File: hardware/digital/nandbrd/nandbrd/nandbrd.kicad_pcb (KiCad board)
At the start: 2 copper layers, 46.9 x 59.8 mm, 14 parts, among them J1 Conn_01x20_Female, J2 Conn_01x20_Male, J3 Conn_01x04_Male, U1 BL652

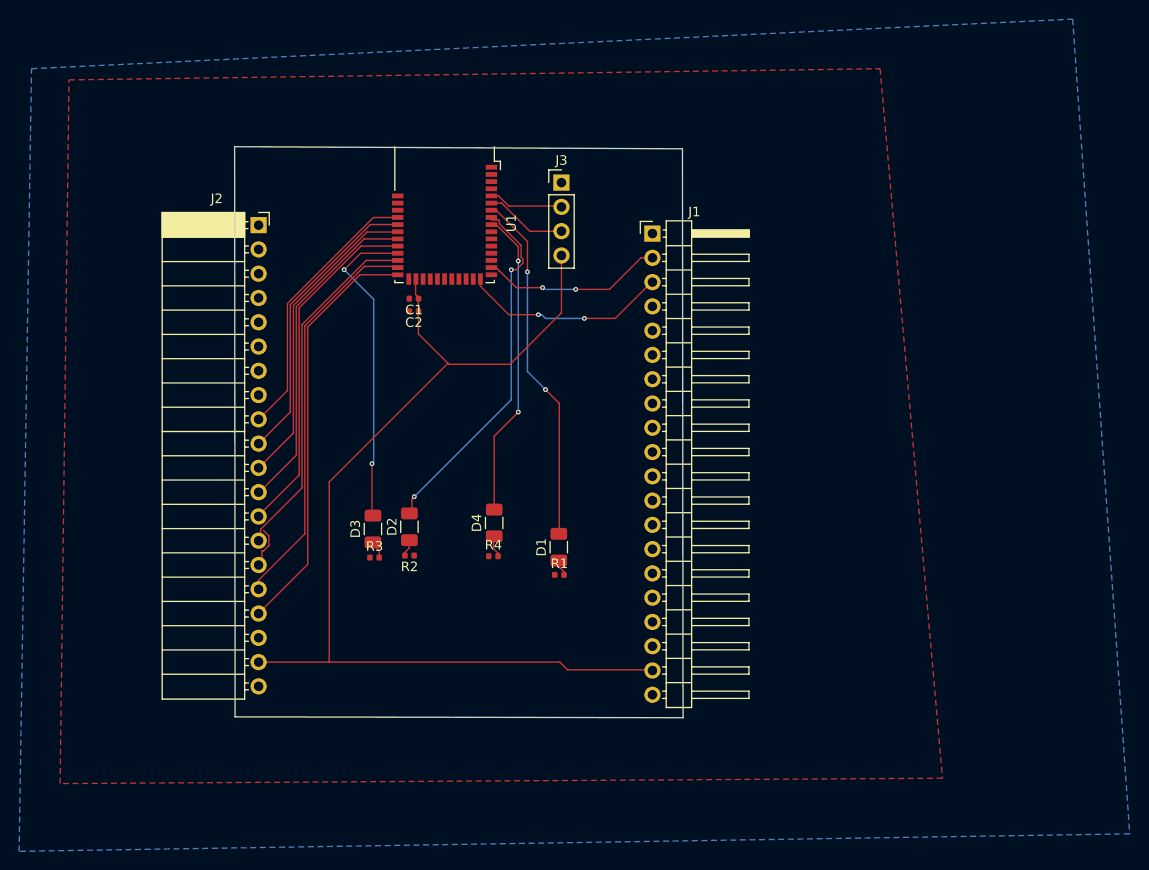
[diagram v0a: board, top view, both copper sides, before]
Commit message: started NAND brd layout. trying to use autorouter
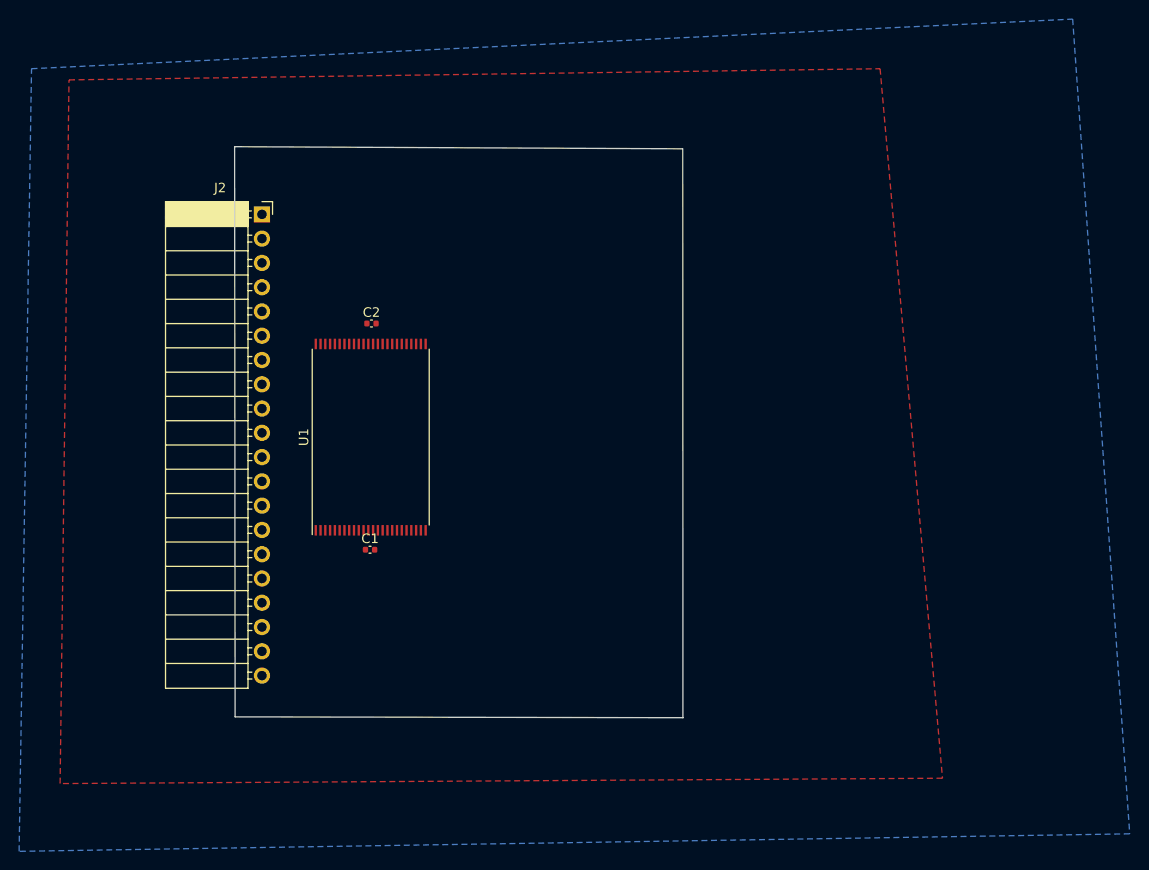
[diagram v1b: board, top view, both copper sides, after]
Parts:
- removed D1, D2, D3, D4: LED, Capacitor_SMD:C_1206_3216Metric
- removed J1: Conn_01x20_Female, Connector_PinHeader_2.54mm:PinHeader_1x20_P2.54mm_Horizontal
- removed J3: Conn_01x04_Male, Connector_PinHeader_2.54mm:PinHeader_1x04_P2.54mm_Vertical
- removed R1, R2, R3, R4: 10kOhm, Resistor_SMD:R_0402_1005Metric
- U1: value BL652 -> MT29F1G08ABAEAWP; footprint RF_Module:Laird_BL652 -> Package_SO:TSOP-I-48_18.4x12mm_P0.5mm
- moved C1 26.7 mm to (133.2, 78.0), turned to 0 degrees
- moved U1 23.7 mm to (133.3, 66.2), turned to 90 degrees
- moved C2 4.62 mm to (133.4, 54.3), turned to 0 degrees
- moved J2 1.18 mm to (121.9, 42.9)
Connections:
- C1 pad 1: +3V3 -> WP
- C2 pad 1: +3V3 -> WP
- J2 pad 10: Net-(J2-Pad10) -> GND
- J2 pad 11: Net-(J2-Pad11) -> D1
- J2 pad 12: Net-(J2-Pad12) -> D0
- J2 pad 13: Net-(J2-Pad13) -> GND
- J2 pad 14: Net-(J2-Pad14) -> CE
- J2 pad 16: Net-(J2-Pad16) -> CLE
- J2 pad 17: Net-(J2-Pad17) -> WE
- J2 pad 18: GND -> RE
- J2 pad 19: +3V3 -> ALE
- J2 pad 2: Net-(J2-Pad2) -> D7
- J2 pad 20: GND -> WP
- J2 pad 3: Net-(J2-Pad3) -> D6
- J2 pad 5: Net-(J2-Pad5) -> D5
- J2 pad 6: Net-(J2-Pad6) -> D4
- J2 pad 7: Net-(J2-Pad7) -> GND
- J2 pad 8: GND -> D3
- J2 pad 9: Net-(J2-Pad9) -> D2
- U1 pad 1: GND -> Net-(U1-Pad1)
- U1 pad 12: Net-(U1-Pad12) -> WP
- U1 pad 13: Net-(U1-Pad13) -> GND
- U1 pad 16: GND -> CLE
- U1 pad 17: Net-(J1-Pad3) -> ALE
- U1 pad 18: Net-(U1-Pad18) -> WE
- U1 pad 19: Net-(U1-Pad19) -> WP
- U1 pad 26: +3V3 -> Net-(U1-Pad26)
- U1 pad 27: GND -> Net-(U1-Pad27)
- U1 pad 28: Net-(J2-Pad17) -> Net-(U1-Pad28)
- U1 pad 29: Net-(J2-Pad16) -> D0
- U1 pad 30: Net-(J2-Pad14) -> D1
- U1 pad 31: Net-(D3-Pad2) -> D2
- U1 pad 32: Net-(J2-Pad13) -> D3
- U1 pad 33: Net-(J2-Pad12) -> Net-(U1-Pad33)
- U1 pad 34: Net-(J2-Pad11) -> Net-(U1-Pad34)
- U1 pad 35: Net-(J2-Pad10) -> Net-(U1-Pad35)
- U1 pad 36: Net-(J2-Pad9) -> GND
- U1 pad 37: Net-(U1-Pad37) -> WP
- U1 pad 39: GND -> Net-(U1-Pad39)
- U1 pad 7: Net-(D1-Pad2) -> (no net)
- U1 pad 8: Net-(D2-Pad2) -> RE
- U1 pad 9: Net-(D4-Pad2) -> CE
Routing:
- net +3V3: track 108.5 -> 0.00 mm
- net Net-(J2-Pad17): track 43.9 -> 0.00 mm
- net Net-(J2-Pad16): track 41.9 -> 0.00 mm
- net Net-(D2-Pad2): track 38.1 -> 0.00 mm, vias 2 -> 0
- net Net-(J2-Pad14): track 37.3 -> 0.00 mm
- net Net-(D1-Pad2): track 37.2 -> 0.00 mm, vias 2 -> 0
- net Net-(J2-Pad13): track 36.6 -> 0.00 mm
- net Net-(J2-Pad12): track 34.4 -> 0.00 mm
- net Net-(D3-Pad2): track 33.8 -> 0.00 mm, vias 2 -> 0
- net Net-(J2-Pad11): track 32.3 -> 0.00 mm
- net Net-(D4-Pad2): track 32.3 -> 0.00 mm, vias 2 -> 0
- net Net-(J2-Pad10): track 30.4 -> 0.00 mm
- net Net-(J2-Pad9): track 28.7 -> 0.00 mm
- net Net-(J1-Pad3): track 21.8 -> 0.00 mm, vias 2 -> 0
- net Net-(U1-Pad15): track 19.2 -> 0.00 mm, vias 2 -> 0
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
